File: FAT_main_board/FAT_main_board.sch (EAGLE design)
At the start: 43 parts, among them IC1 74LS241N

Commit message: [FAT board] Change some names.
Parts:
- removed BAT_SIG2: (no value), con-ptr500:AK300/2
- renumbered SV1 to DYN1, SV3 to DYN2, SV4 to DYN3
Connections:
- net GND: now also U$1.GND2
- net N$20: no longer BAT_SIG2-1.KL
- net N$25: no longer BAT_SIG2-2.KL
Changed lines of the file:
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@@
 <part name="IC1" library="74xx-eu" deviceset="74*241" device="N" technology="LS"/>
 <part name="R4" library="resistor" deviceset="R-EU_" device="0204/7" value="10K"/>
-<part name="SV1" library="con-lstb" deviceset="MA03-1" device=""/>
+<part name="DYN1" library="con-lstb" deviceset="MA03-1" device=""/>
 <part name="UART1" library="con-lstb" deviceset="MA04-1" device=""/>
 <part name="UART2" library="con-lstb" deviceset="MA04-1" device=""/>
@@
 <part name="BAT_POWER2" library="con-ptr500" deviceset="AK300/2" device=""/>
 <part name="BAT_SIG1" library="con-ptr500" deviceset="AK300/2" device=""/>
-<part name="BAT_SIG2" library="con-ptr500" deviceset="AK300/2" device=""/>
-<part name="SV3" library="con-lstb" deviceset="MA03-1" device=""/>
-<part name="SV4" library="con-lstb" deviceset="MA03-1" device=""/>
+<part name="DYN2" library="con-lstb" deviceset="MA03-1" device=""/>
+<part name="DYN3" library="con-lstb" deviceset="MA03-1" device=""/>
 <part name="JP1" library="pinhead" deviceset="PINHD-1X2" device=""/>
 <part name="R5" library="rcl" deviceset="R-EU_" device="0204/7" value="5k"/>
@@
 <instance part="IC1" gate="P" x="109.22" y="-132.08"/>
 <instance part="R4" gate="G$1" x="119.38" y="-99.06" rot="R90"/>
-<instance part="SV1" gate="G$1" x="213.36" y="-116.84" rot="R180"/>
+<instance part="DYN1" gate="G$1" x="213.36" y="-116.84" rot="R180"/>
 <instance part="UART1" gate="1" x="-111.76" y="25.4"/>
 <instance part="UART2" gate="1" x="-111.76" y="7.62"/>
@@
 <instance part="BAT_SIG1" gate="-1" x="-96.52" y="104.14"/>
 <instance part="BAT_SIG1" gate="-2" x="-96.52" y="99.06"/>
-<instance part="BAT_SIG2" gate="-1" x="-96.52" y="124.46"/>
-<instance part="BAT_SIG2" gate="-2" x="-96.52" y="119.38"/>
-<instance part="SV3" gate="G$1" x="213.36" y="-132.08" rot="R180"/>
-<instance part="SV4" gate="G$1" x="213.36" y="-147.32" rot="R180"/>
+<instance part="DYN2" gate="G$1" x="213.36" y="-132.08" rot="R180"/>
+<instance part="DYN3" gate="G$1" x="213.36" y="-147.32" rot="R180"/>
 <instance part="JP1" gate="G$1" x="40.64" y="-66.04"/>
 <instance part="R5" gate="G$1" x="0" y="-58.42"/>
@@
 </segment>
 <segment>
-<pinref part="SV1" gate="G$1" pin="1"/>
+<pinref part="DYN1" gate="G$1" pin="1"/>
 <wire x1="205.74" y1="-114.3" x2="203.2" y2="-114.3" width="0.1524" layer="91"/>
 <label x="182.88" y="-114.3" size="1.778" layer="95"/>
-<pinref part="SV3" gate="G$1" pin="1"/>
+<pinref part="DYN2" gate="G$1" pin="1"/>
 <wire x1="203.2" y1="-114.3" x2="182.88" y2="-114.3" width="0.1524" layer="91"/>
 <wire x1="205.74" y1="-129.54" x2="203.2" y2="-129.54" width="0.1524" layer="91"/>
 <wire x1="203.2" y1="-129.54" x2="203.2" y2="-114.3" width="0.1524" layer="91"/>
 <junction x="203.2" y="-114.3"/>
-<pinref part="SV4" gate="G$1" pin="1"/>
+<pinref part="DYN3" gate="G$1" pin="1"/>
 <wire x1="205.74" y1="-144.78" x2="203.2" y2="-144.78" width="0.1524" layer="91"/>
 <wire x1="203.2" y1="-144.78" x2="203.2" y2="-129.54" width="0.1524" layer="91"/>
@@
 <wire x1="20.32" y1="-58.42" x2="27.94" y2="-58.42" width="0.1524" layer="91"/>
 <wire x1="27.94" y1="-58.42" x2="27.94" y2="-66.04" width="0.1524" layer="91"/>
+</segment>
+<segment>
+<pinref part="U$1" gate="G$1" pin="GND2"/>
+<wire x1="20.32" y1="-12.7" x2="25.4" y2="-12.7" width="0.1524" layer="91"/>
+<label x="22.86" y="-12.7" size="1.778" layer="95"/>
 </segment>
 </net>
@@
 </segment>
 <segment>
-<pinref part="SV1" gate="G$1" pin="3"/>
+<pinref part="DYN1" gate="G$1" pin="3"/>
 <wire x1="205.74" y1="-119.38" x2="198.12" y2="-119.38" width="0.1524" layer="91"/>
 <label x="182.88" y="-119.38" size="1.778" layer="95"/>
-<pinref part="SV4" gate="G$1" pin="3"/>
+<pinref part="DYN3" gate="G$1" pin="3"/>
 <wire x1="198.12" y1="-119.38" x2="182.88" y2="-119.38" width="0.1524" layer="91"/>
 <wire x1="205.74" y1="-149.86" x2="198.12" y2="-149.86" width="0.1524" layer="91"/>
 <wire x1="198.12" y1="-149.86" x2="198.12" y2="-134.62" width="0.1524" layer="91"/>
 <junction x="198.12" y="-119.38"/>
-<pinref part="SV3" gate="G$1" pin="3"/>
+<pinref part="DYN2" gate="G$1" pin="3"/>
 <wire x1="198.12" y1="-134.62" x2="198.12" y2="-119.38" width="0.1524" layer="91"/>
 <wire x1="205.74" y1="-134.62" x2="198.12" y2="-134.62" width="0.1524" layer="91"/>
@@
 <net name="10V_POWER" class="0">
 <segment>
-<pinref part="SV1" gate="G$1" pin="2"/>
+<pinref part="DYN1" gate="G$1" pin="2"/>
 <wire x1="205.74" y1="-116.84" x2="200.66" y2="-116.84" width="0.1524" layer="91"/>
 <label x="182.88" y="-116.84" size="1.778" layer="95"/>
-<pinref part="SV3" gate="G$1" pin="2"/>
+<pinref part="DYN2" gate="G$1" pin="2"/>
 <wire x1="200.66" y1="-116.84" x2="182.88" y2="-116.84" width="0.1524" layer="91"/>
 <wire x1="205.74" y1="-132.08" x2="200.66" y2="-132.08" width="0.1524" layer="91"/>
 <wire x1="200.66" y1="-132.08" x2="200.66" y2="-116.84" width="0.1524" layer="91"/>
 <junction x="200.66" y="-116.84"/>
-<pinref part="SV4" gate="G$1" pin="2"/>
+<pinref part="DYN3" gate="G$1" pin="2"/>
 <wire x1="205.74" y1="-147.32" x2="200.66" y2="-147.32" width="0.1524" layer="91"/>
 <wire x1="200.66" y1="-147.32" x2="200.66" y2="-132.08" width="0.1524" layer="91"/>
@@
 <wire x1="-88.9" y1="104.14" x2="-88.9" y2="114.3" width="0.1524" layer="91"/>
 <junction x="-88.9" y="114.3"/>
-<pinref part="BAT_SIG2" gate="-1" pin="KL"/>
-<wire x1="-91.44" y1="124.46" x2="-88.9" y2="124.46" width="0.1524" layer="91"/>
-<wire x1="-88.9" y1="124.46" x2="-88.9" y2="114.3" width="0.1524" layer="91"/>
 </segment>
 </net>
@@
 <wire x1="-86.36" y1="99.06" x2="-86.36" y2="109.22" width="0.1524" layer="91"/>
 <junction x="-86.36" y="109.22"/>
-<pinref part="BAT_SIG2" gate="-2" pin="KL"/>
-<wire x1="-91.44" y1="119.38" x2="-86.36" y2="119.38" width="0.1524" layer="91"/>
-<wire x1="-86.36" y1="119.38" x2="-86.36" y2="109.22" width="0.1524" layer="91"/>
-</segment>
-</net>
+</segment>
+</net>

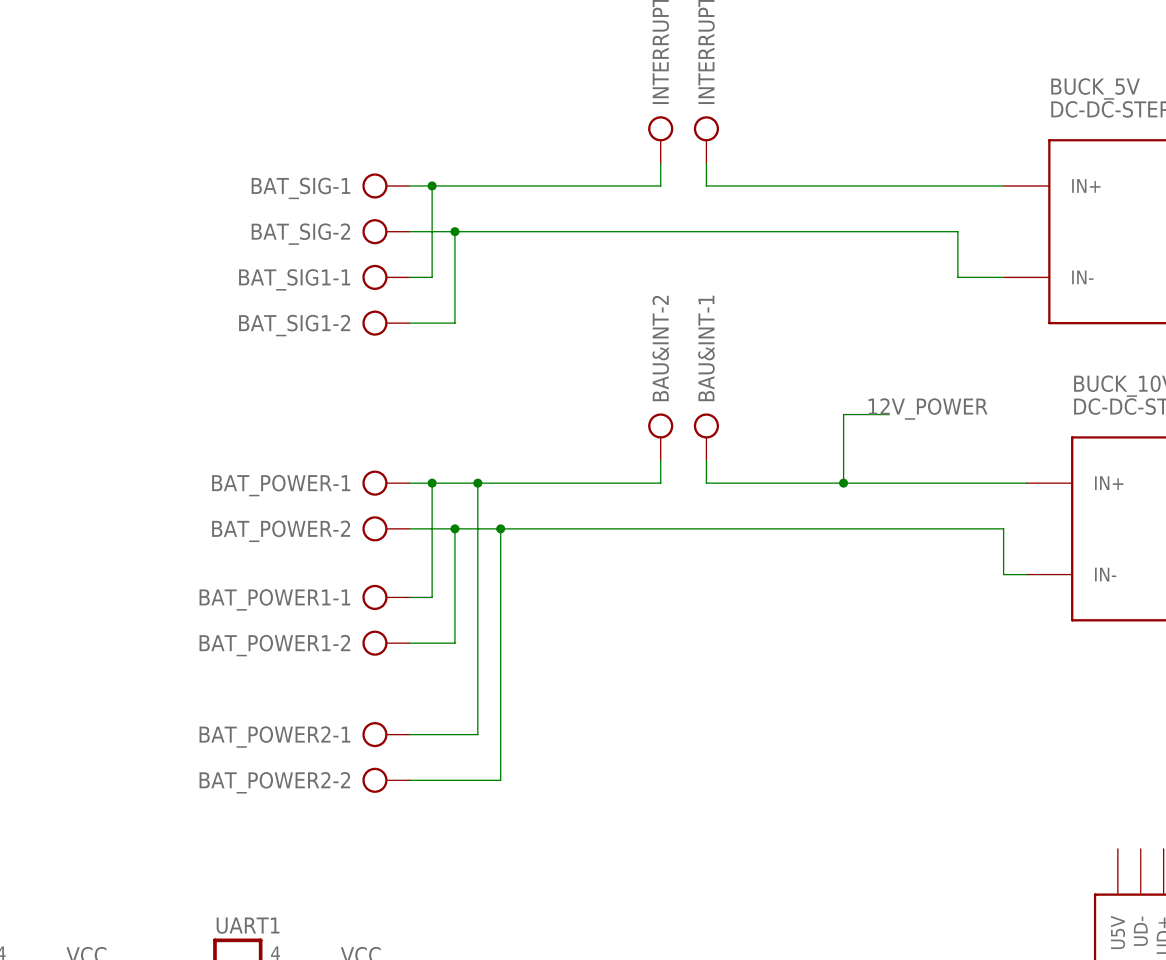
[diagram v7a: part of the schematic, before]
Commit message: [FAT board] Connect additionnal power connectors behind interruptors.
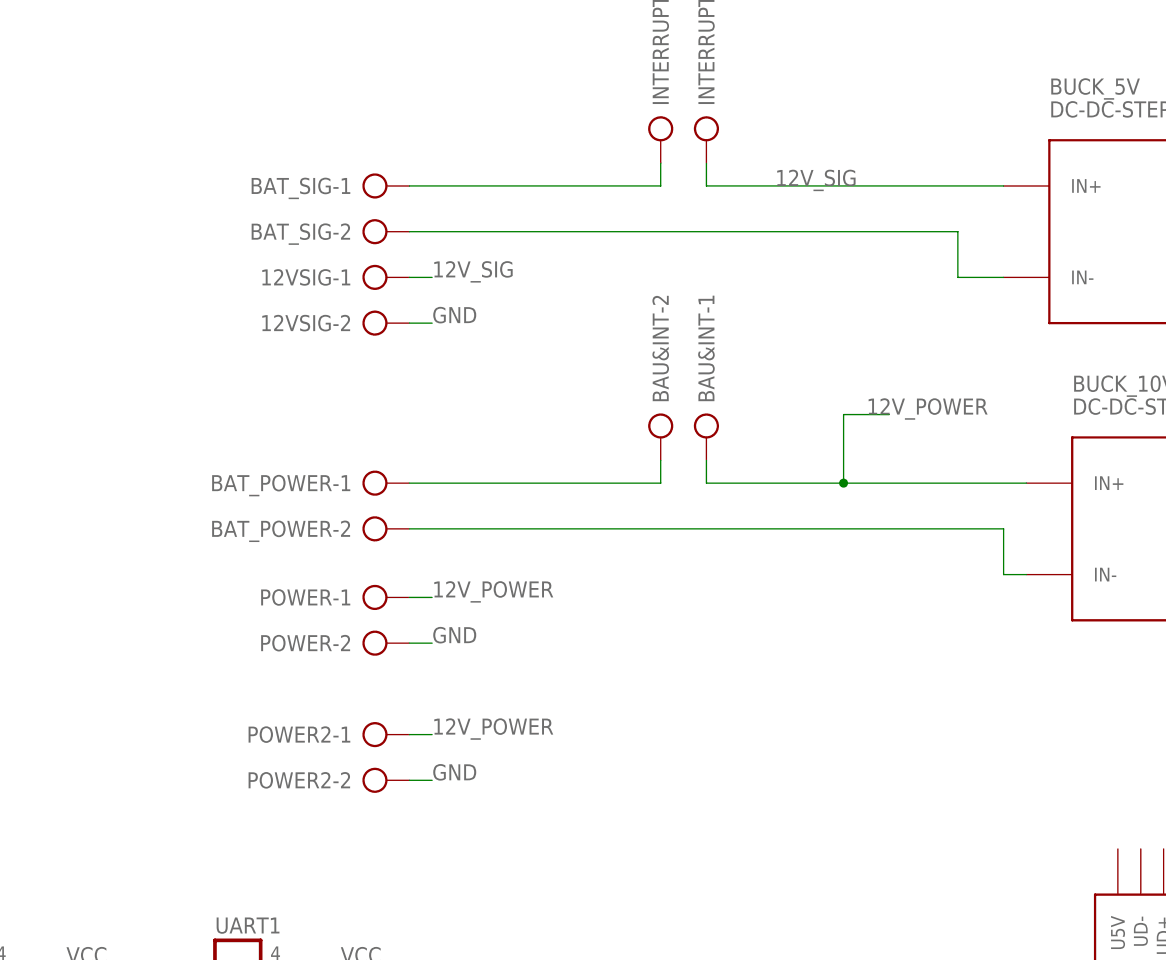
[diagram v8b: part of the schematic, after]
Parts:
- renumbered BAT_POWER1 to POWER, BAT_POWER2 to POWER2, BAT_SIG1 to 12VSIG
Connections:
- removed net N$22: BUCK_5V.IN+, INTERRUPTOR-1.KL
- new net 12V_SIG: 12VSIG-1.KL, BUCK_5V.IN+, INTERRUPTOR-1.KL
- net 12V_POWER: now also POWER-1.KL, POWER2-1.KL
- net GND: now also 12VSIG-2.KL, POWER-2.KL, POWER2-2.KL
- net N$13: no longer POWER-1.KL, POWER2-1.KL
- net N$20: no longer 12VSIG-1.KL
- net N$23: no longer POWER-2.KL, POWER2-2.KL
- net N$25: no longer 12VSIG-2.KL
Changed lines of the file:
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@@
 <part name="BUCK_10V" library="diy-modules" deviceset="DC-DC-STEP-DOWN-LM2596" device=""/>
 <part name="BUCK_5V" library="diy-modules" deviceset="DC-DC-STEP-DOWN-LM2596" device=""/>
-<part name="BAT_POWER1" library="con-ptr500" deviceset="AK300/2" device=""/>
-<part name="BAT_POWER2" library="con-ptr500" deviceset="AK300/2" device=""/>
-<part name="BAT_SIG1" library="con-ptr500" deviceset="AK300/2" device=""/>
+<part name="POWER" library="con-ptr500" deviceset="AK300/2" device=""/>
+<part name="POWER2" library="con-ptr500" deviceset="AK300/2" device=""/>
+<part name="12VSIG" library="con-ptr500" deviceset="AK300/2" device=""/>
 <part name="DYN2" library="con-lstb" deviceset="MA03-1" device=""/>
 <part name="DYN3" library="con-lstb" deviceset="MA03-1" device=""/>
@@
 <instance part="BUCK_10V" gate="G$1" x="-5.08" y="76.2"/>
 <instance part="BUCK_5V" gate="G$1" x="-7.62" y="109.22"/>
-<instance part="BAT_POWER1" gate="-1" x="-96.52" y="68.58"/>
-<instance part="BAT_POWER1" gate="-2" x="-96.52" y="63.5"/>
-<instance part="BAT_POWER2" gate="-1" x="-96.52" y="53.34"/>
-<instance part="BAT_POWER2" gate="-2" x="-96.52" y="48.26"/>
-<instance part="BAT_SIG1" gate="-1" x="-96.52" y="104.14"/>
-<instance part="BAT_SIG1" gate="-2" x="-96.52" y="99.06"/>
+<instance part="POWER" gate="-1" x="-96.52" y="68.58"/>
+<instance part="POWER" gate="-2" x="-96.52" y="63.5"/>
+<instance part="POWER2" gate="-1" x="-96.52" y="53.34"/>
+<instance part="POWER2" gate="-2" x="-96.52" y="48.26"/>
+<instance part="12VSIG" gate="-1" x="-96.52" y="104.14"/>
+<instance part="12VSIG" gate="-2" x="-96.52" y="99.06"/>
 <instance part="DYN2" gate="G$1" x="213.36" y="-132.08" rot="R180"/>
 <instance part="DYN3" gate="G$1" x="213.36" y="-147.32" rot="R180"/>
@@
 <label x="22.86" y="-12.7" size="1.778" layer="95"/>
 </segment>
+<segment>
+<pinref part="POWER2" gate="-2" pin="KL"/>
+<wire x1="-91.44" y1="48.26" x2="-88.9" y2="48.26" width="0.1524" layer="91"/>
+<label x="-88.9" y="48.26" size="1.778" layer="95"/>
+</segment>
+<segment>
+<pinref part="POWER" gate="-2" pin="KL"/>
+<wire x1="-91.44" y1="63.5" x2="-88.9" y2="63.5" width="0.1524" layer="91"/>
+<label x="-88.9" y="63.5" size="1.778" layer="95"/>
+</segment>
+<segment>
+<pinref part="12VSIG" gate="-2" pin="KL"/>
+<wire x1="-91.44" y1="99.06" x2="-88.9" y2="99.06" width="0.1524" layer="91"/>
+<label x="-88.9" y="99.06" size="1.778" layer="95"/>
+</segment>
 </net>
 <net name="VCC" class="0">
@@
 <wire x1="-43.18" y1="88.9" x2="-38.1" y2="88.9" width="0.1524" layer="91"/>
 <label x="-40.64" y="88.9" size="1.778" layer="95"/>
+</segment>
+<segment>
+<pinref part="POWER2" gate="-1" pin="KL"/>
+<wire x1="-91.44" y1="53.34" x2="-88.9" y2="53.34" width="0.1524" layer="91"/>
+<label x="-88.9" y="53.34" size="1.778" layer="95"/>
+</segment>
+<segment>
+<pinref part="POWER" gate="-1" pin="KL"/>
+<wire x1="-91.44" y1="68.58" x2="-88.9" y2="68.58" width="0.1524" layer="91"/>
+<label x="-88.9" y="68.58" size="1.778" layer="95"/>
 </segment>
 </net>
@@
 <pinref part="BAT_POWER" gate="-1" pin="KL"/>
 <pinref part="BAU&amp;INT" gate="-2" pin="KL"/>
-<wire x1="-91.44" y1="81.28" x2="-88.9" y2="81.28" width="0.1524" layer="91"/>
-<wire x1="-88.9" y1="81.28" x2="-83.82" y2="81.28" width="0.1524" layer="91"/>
-<wire x1="-83.82" y1="81.28" x2="-63.5" y2="81.28" width="0.1524" layer="91"/>
+<wire x1="-91.44" y1="81.28" x2="-63.5" y2="81.28" width="0.1524" layer="91"/>
 <wire x1="-63.5" y1="81.28" x2="-63.5" y2="83.82" width="0.1524" layer="91"/>
-<pinref part="BAT_POWER1" gate="-1" pin="KL"/>
-<wire x1="-91.44" y1="68.58" x2="-88.9" y2="68.58" width="0.1524" layer="91"/>
-<wire x1="-88.9" y1="68.58" x2="-88.9" y2="81.28" width="0.1524" layer="91"/>
-<junction x="-88.9" y="81.28"/>
-<pinref part="BAT_POWER2" gate="-1" pin="KL"/>
-<wire x1="-91.44" y1="53.34" x2="-83.82" y2="53.34" width="0.1524" layer="91"/>
-<wire x1="-83.82" y1="53.34" x2="-83.82" y2="81.28" width="0.1524" layer="91"/>
-<junction x="-83.82" y="81.28"/>
 </segment>
 </net>
@@
 <pinref part="BAT_SIG" gate="-1" pin="KL"/>
 <pinref part="INTERRUPTOR" gate="-2" pin="KL"/>
-<wire x1="-91.44" y1="114.3" x2="-88.9" y2="114.3" width="0.1524" layer="91"/>
-<wire x1="-88.9" y1="114.3" x2="-63.5" y2="114.3" width="0.1524" layer="91"/>
+<wire x1="-91.44" y1="114.3" x2="-63.5" y2="114.3" width="0.1524" layer="91"/>
 <wire x1="-63.5" y1="114.3" x2="-63.5" y2="116.84" width="0.1524" layer="91"/>
-<pinref part="BAT_SIG1" gate="-1" pin="KL"/>
-<wire x1="-91.44" y1="104.14" x2="-88.9" y2="104.14" width="0.1524" layer="91"/>
-<wire x1="-88.9" y1="104.14" x2="-88.9" y2="114.3" width="0.1524" layer="91"/>
-<junction x="-88.9" y="114.3"/>
-</segment>
-</net>
-<net name="N$22" class="0">
+</segment>
+</net>
+<net name="12V_SIG" class="0">
 <segment>
 <pinref part="INTERRUPTOR" gate="-1" pin="KL"/>
@@
 <pinref part="BUCK_5V" gate="G$1" pin="IN+"/>
 <wire x1="-58.42" y1="114.3" x2="-25.4" y2="114.3" width="0.1524" layer="91"/>
+<label x="-50.8" y="114.3" size="1.778" layer="95"/>
+</segment>
+<segment>
+<pinref part="12VSIG" gate="-1" pin="KL"/>
+<wire x1="-91.44" y1="104.14" x2="-88.9" y2="104.14" width="0.1524" layer="91"/>
+<label x="-88.9" y="104.14" size="1.778" layer="95"/>
 </segment>
 </net>
@@
 <segment>
 <pinref part="BAT_POWER" gate="-2" pin="KL"/>
-<wire x1="-91.44" y1="76.2" x2="-86.36" y2="76.2" width="0.1524" layer="91"/>
-<wire x1="-86.36" y1="76.2" x2="-81.28" y2="76.2" width="0.1524" layer="91"/>
-<wire x1="-81.28" y1="76.2" x2="-25.4" y2="76.2" width="0.1524" layer="91"/>
+<wire x1="-91.44" y1="76.2" x2="-25.4" y2="76.2" width="0.1524" layer="91"/>
 <wire x1="-25.4" y1="76.2" x2="-25.4" y2="71.12" width="0.1524" layer="91"/>
 <pinref part="BUCK_10V" gate="G$1" pin="IN-"/>
 <wire x1="-25.4" y1="71.12" x2="-22.86" y2="71.12" width="0.1524" layer="91"/>
-<pinref part="BAT_POWER1" gate="-2" pin="KL"/>
-<wire x1="-91.44" y1="63.5" x2="-86.36" y2="63.5" width="0.1524" layer="91"/>
-<wire x1="-86.36" y1="63.5" x2="-86.36" y2="76.2" width="0.1524" layer="91"/>
-<junction x="-86.36" y="76.2"/>
-<pinref part="BAT_POWER2" gate="-2" pin="KL"/>
-<wire x1="-91.44" y1="48.26" x2="-81.28" y2="48.26" width="0.1524" layer="91"/>
-<wire x1="-81.28" y1="48.26" x2="-81.28" y2="76.2" width="0.1524" layer="91"/>
-<junction x="-81.28" y="76.2"/>
 </segment>
 </net>
@@
 <segment>
 <pinref part="BAT_SIG" gate="-2" pin="KL"/>
-<wire x1="-91.44" y1="109.22" x2="-86.36" y2="109.22" width="0.1524" layer="91"/>
-<wire x1="-86.36" y1="109.22" x2="-30.48" y2="109.22" width="0.1524" layer="91"/>
+<wire x1="-91.44" y1="109.22" x2="-30.48" y2="109.22" width="0.1524" layer="91"/>
 <wire x1="-30.48" y1="109.22" x2="-30.48" y2="104.14" width="0.1524" layer="91"/>
 <pinref part="BUCK_5V" gate="G$1" pin="IN-"/>
 <wire x1="-30.48" y1="104.14" x2="-25.4" y2="104.14" width="0.1524" layer="91"/>
-<pinref part="BAT_SIG1" gate="-2" pin="KL"/>
-<wire x1="-91.44" y1="99.06" x2="-86.36" y2="99.06" width="0.1524" layer="91"/>
-<wire x1="-86.36" y1="99.06" x2="-86.36" y2="109.22" width="0.1524" layer="91"/>
-<junction x="-86.36" y="109.22"/>
-</segment>
-</net>
+</segment>
+</net>
